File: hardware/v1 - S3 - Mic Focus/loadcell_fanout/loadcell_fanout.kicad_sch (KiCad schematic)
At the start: 18 parts, among them J1 Conn_01x05, J2 EXP, U2 L, U3 R

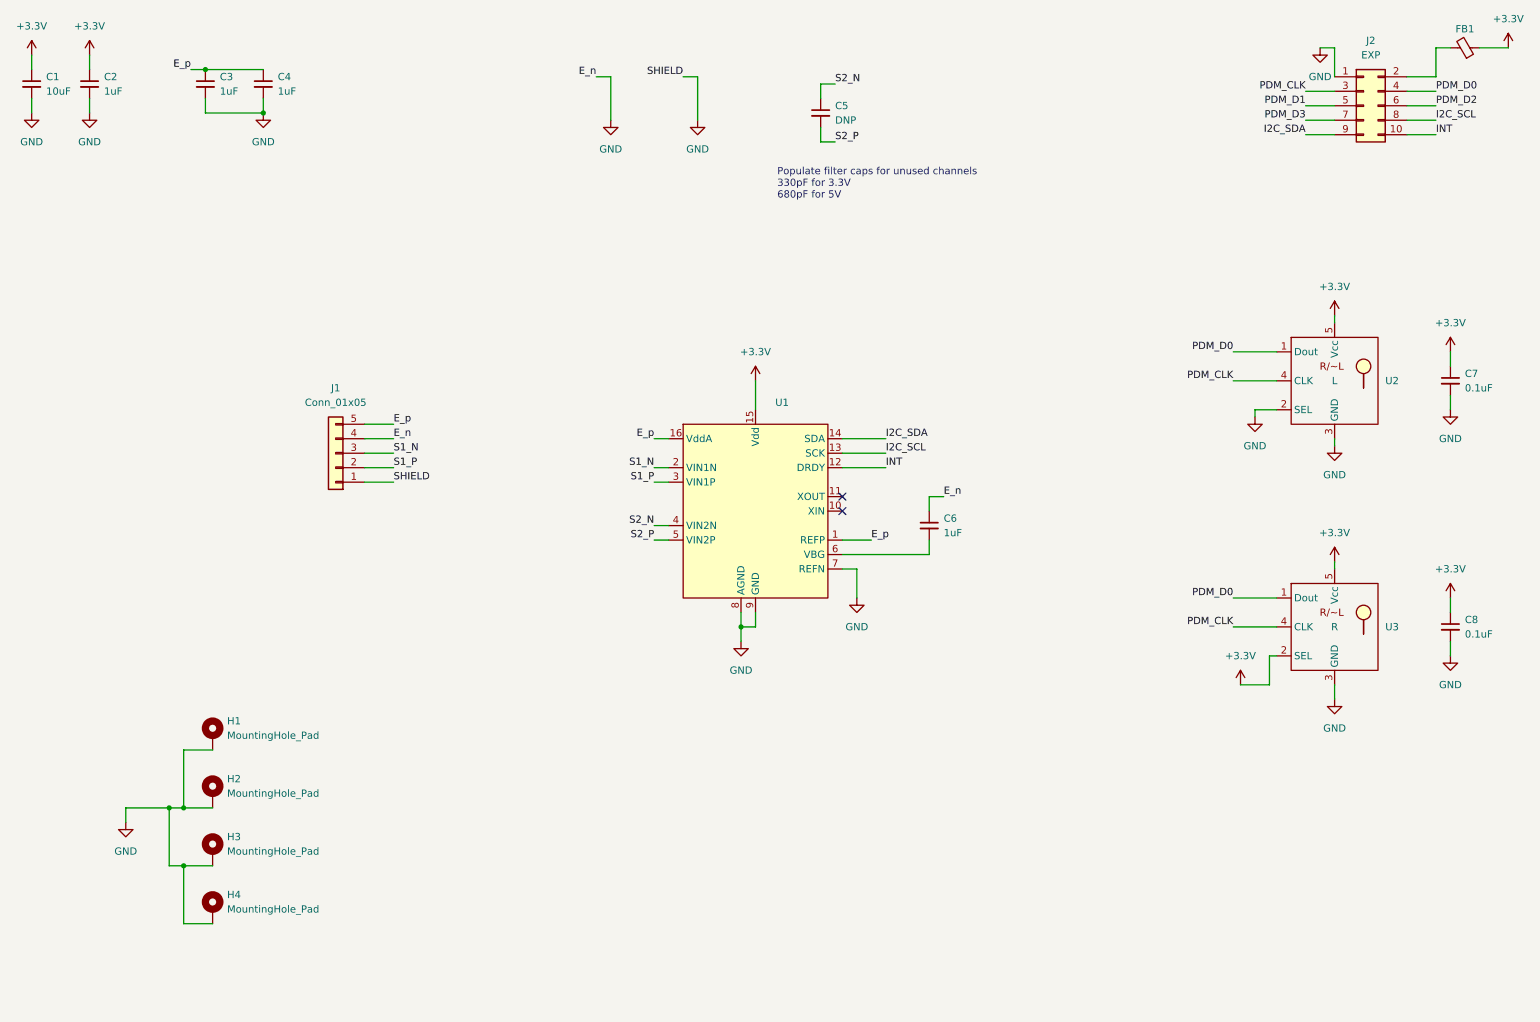
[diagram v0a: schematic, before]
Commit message: Standoff move, silkscreen work
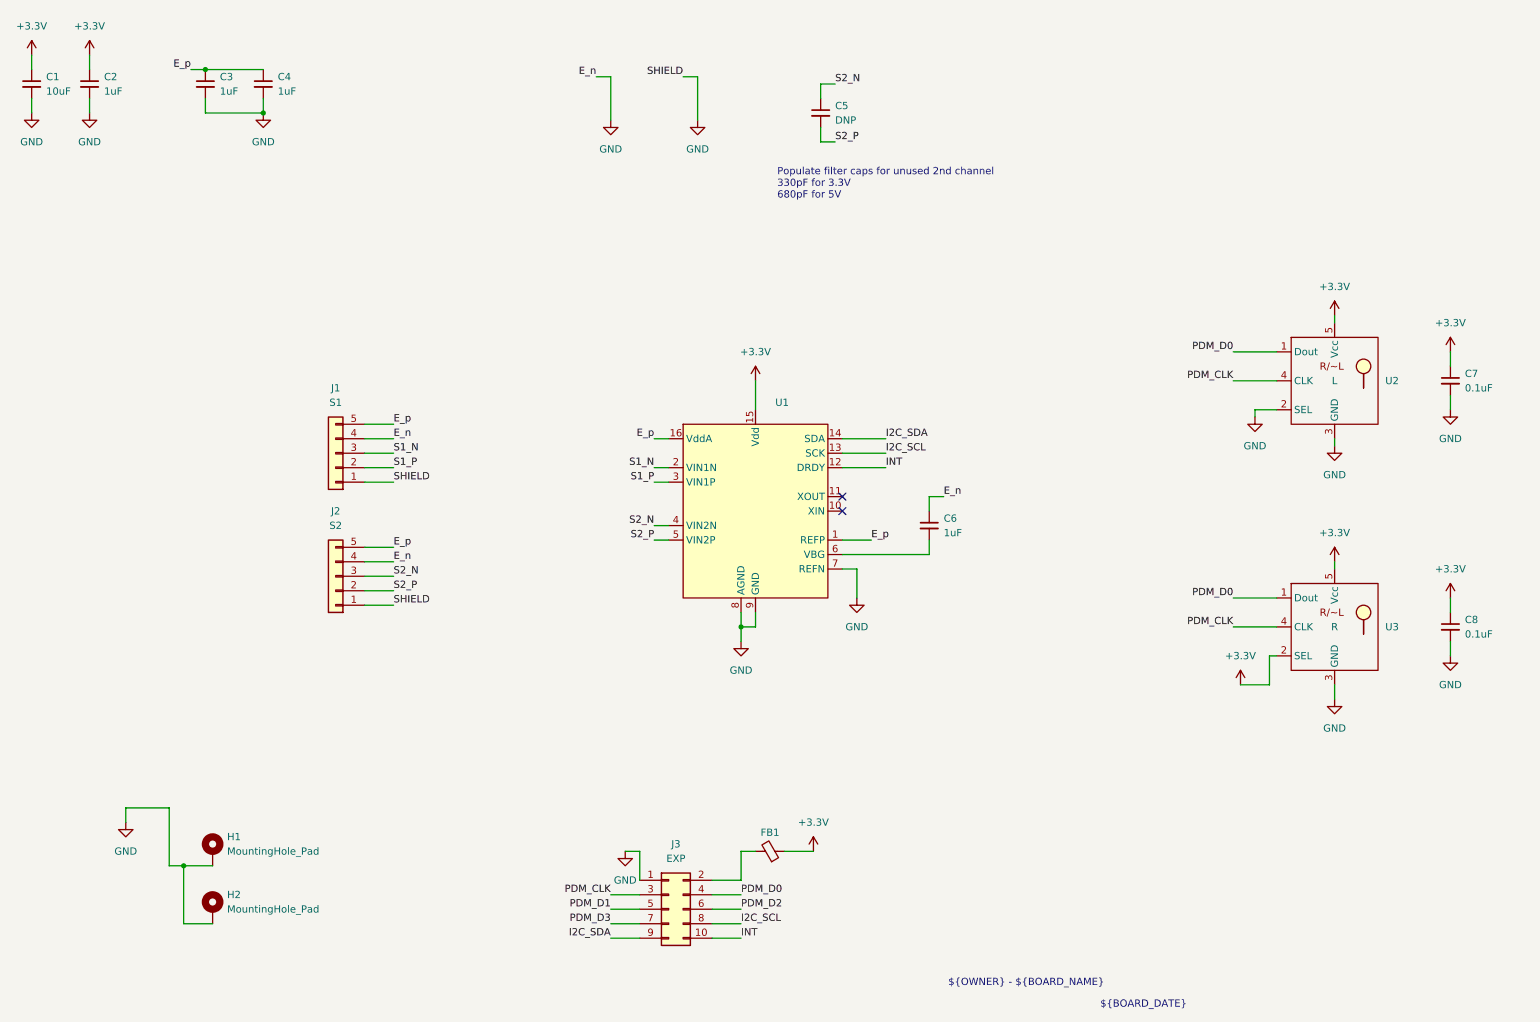
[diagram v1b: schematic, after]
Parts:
- removed H1, H2: MountingHole_Pad, MountingHole:MountingHole_2.2mm_M2_DIN965_Pad, symbol Mechanical:MountingHole_Pad
- added J2: S2, Connector_PinHeader_2.54mm:PinHeader_1x05_P2.54mm_Vertical, symbol Connector_Generic:Conn_01x05
- J1: value Conn_01x05 -> S1
- renumbered H3 to H1, H4 to H2, J2 to J3
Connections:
- net E_p: now also J2.5 (Pin_5)
- net GND: now also J2.1 (Pin_1), J2.4 (Pin_4)
- net S2_N: now also J2.3 (Pin_3)
- net S2_P: now also J2.2 (Pin_2)
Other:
- note added: "${BOARD_DATE}"
- note added: "${OWNER} - ${BOARD_NAME}"
- note added: "Populate filter caps for unused 2nd channel 330pF for 3.3V 680pF for 5V"
- note removed: "Populate filter caps for unused channels 330pF for 3.3V 680pF for 5V"
- moved on the sheet: FB1, J3
